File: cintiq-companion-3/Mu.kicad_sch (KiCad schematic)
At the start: 12 parts, among them J1 Conn_01x03_Pin

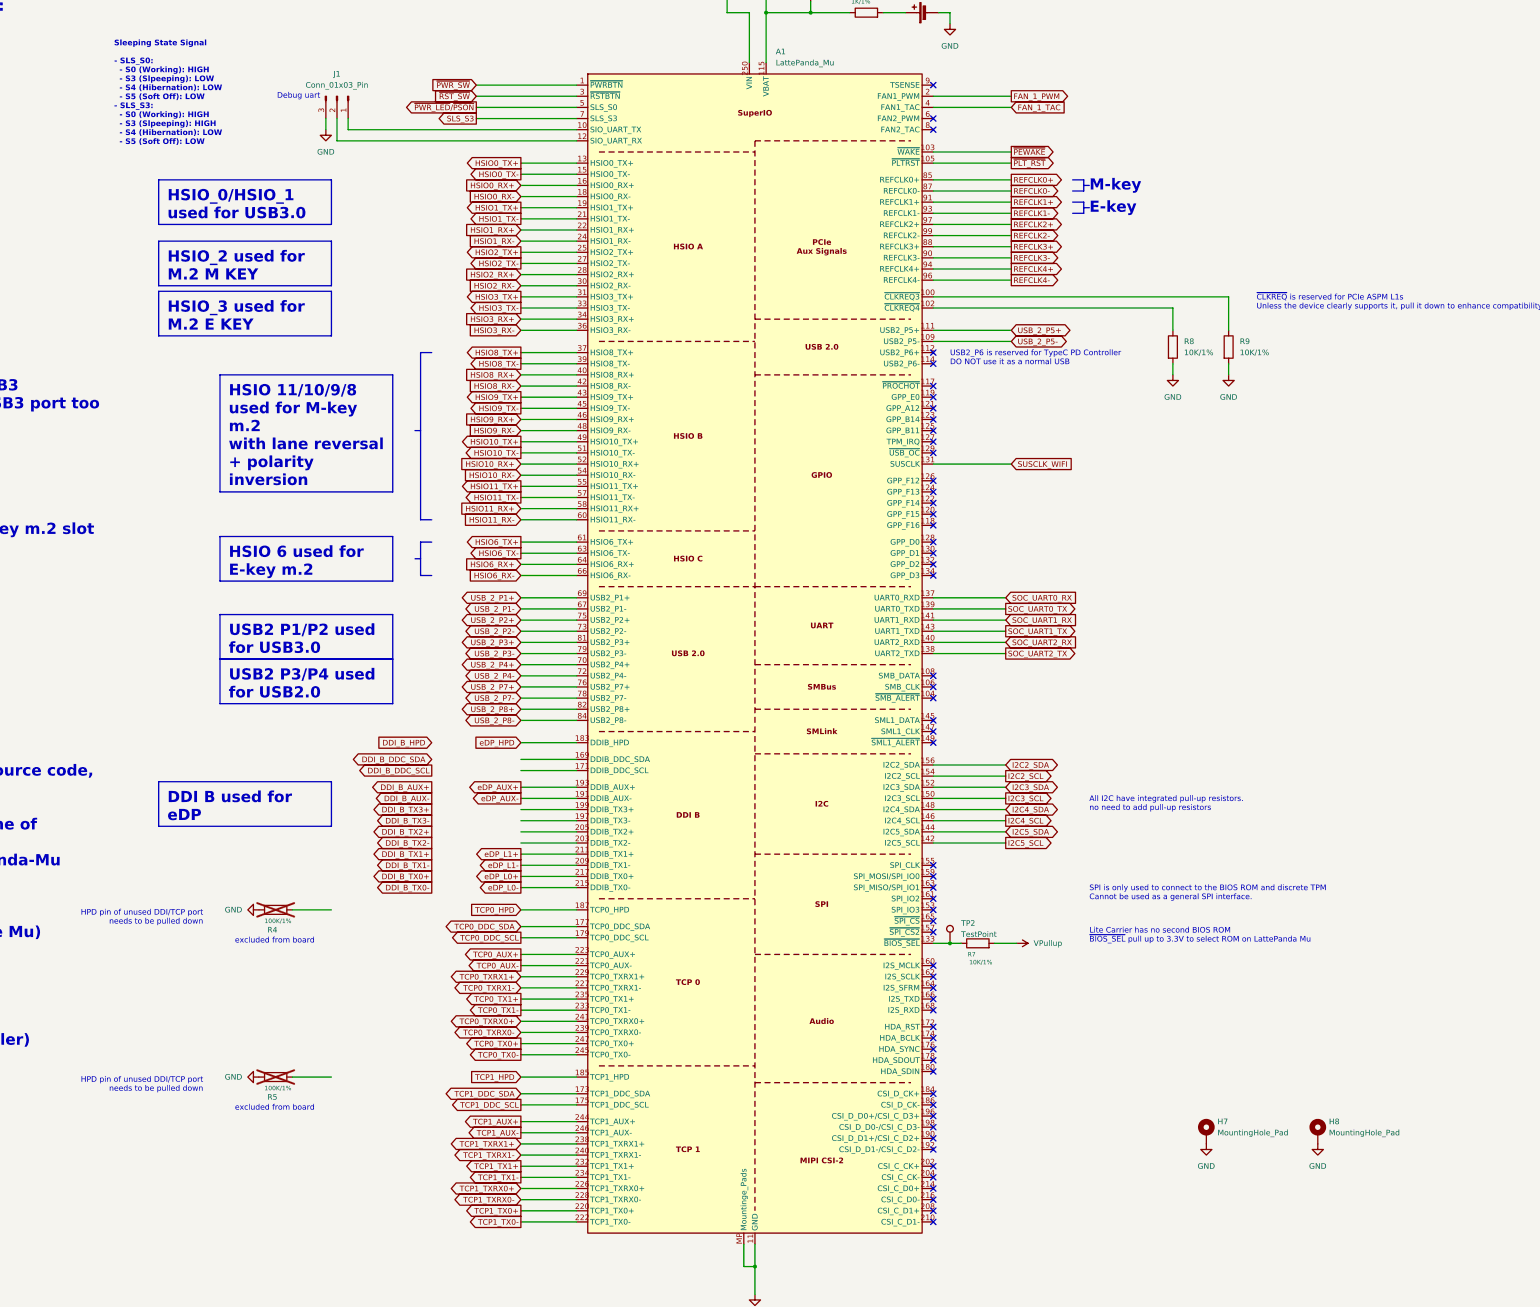
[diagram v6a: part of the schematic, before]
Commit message: Disconnected so far unused things on schematic
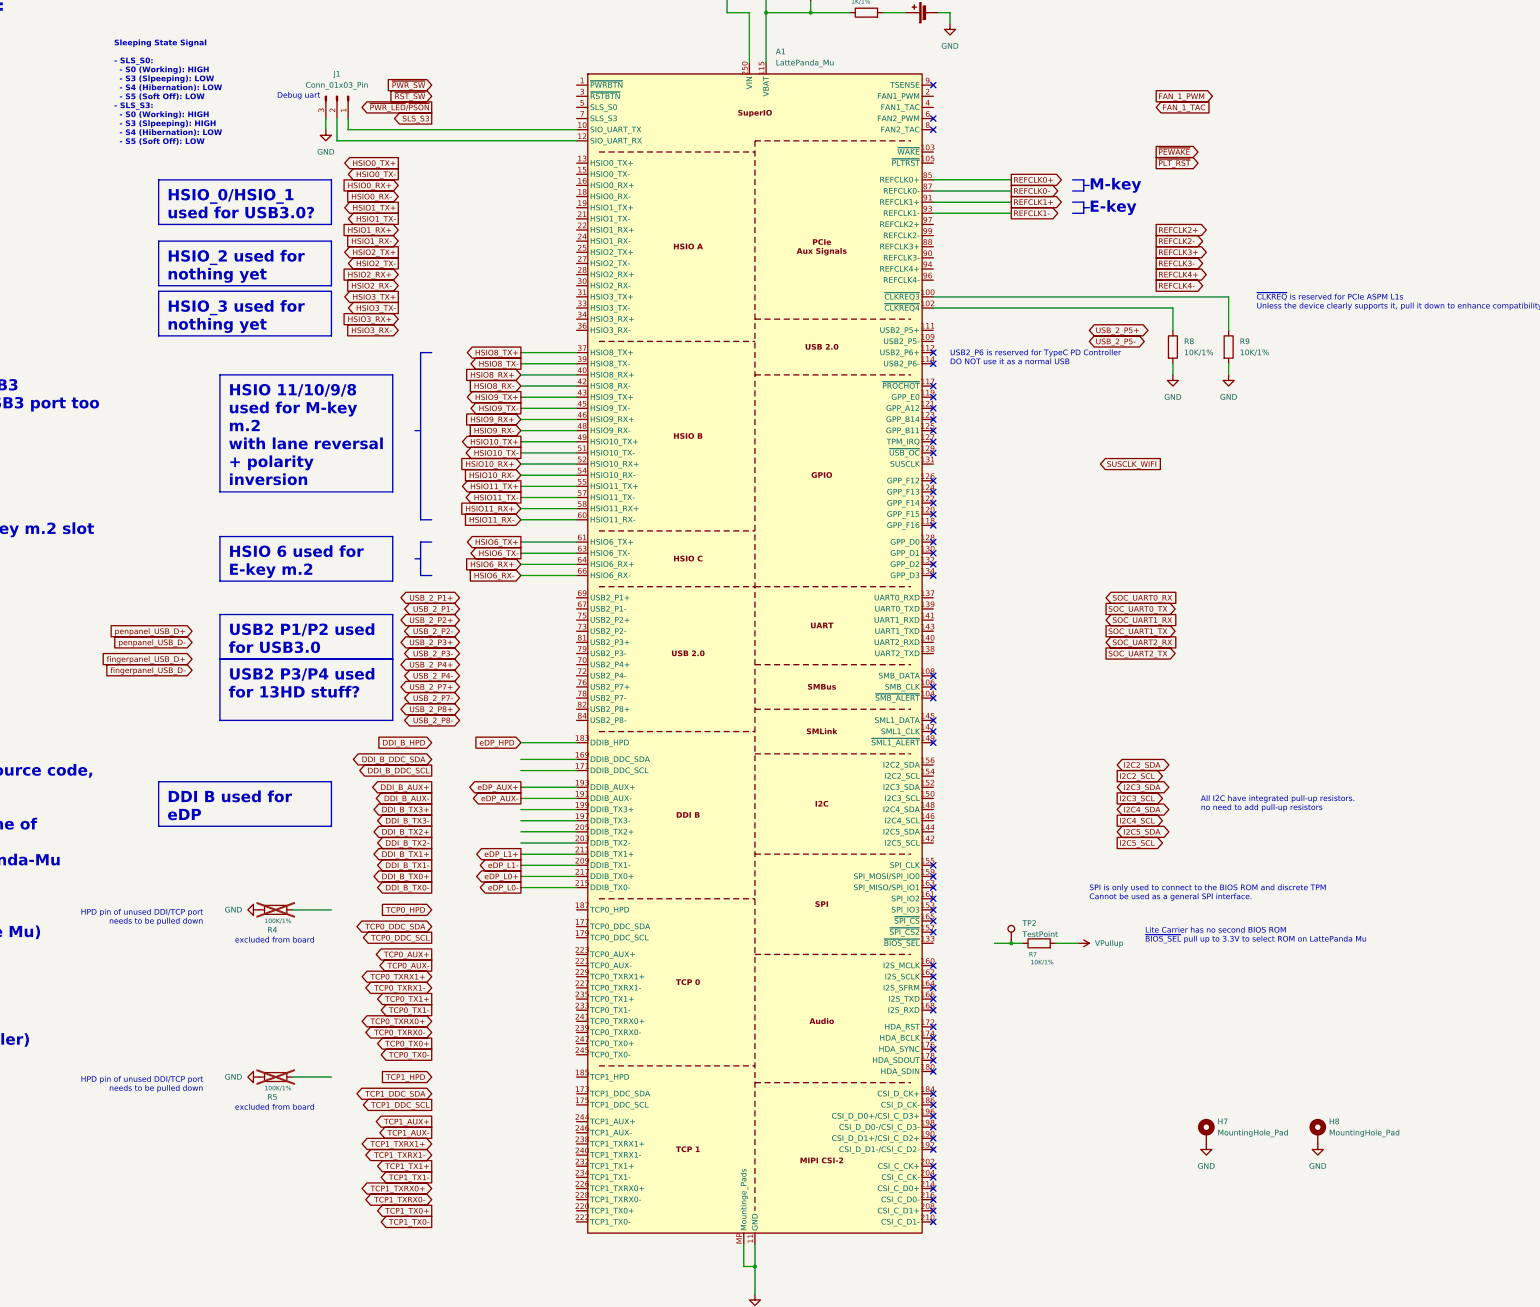
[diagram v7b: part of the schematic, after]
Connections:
- net FAN_1_PWM: no longer A1.2 (FAN1_PWM)
- net FAN_1_TAC: no longer A1.4 (FAN1_TAC)
- net HSIO0_RX+: no longer A1.16 (HSIO0_RX+)
- net HSIO0_RX-: no longer A1.18 (HSIO0_RX-)
- net HSIO0_TX+: no longer A1.13 (HSIO0_TX+)
- net HSIO0_TX-: no longer A1.15 (HSIO0_TX-)
- net HSIO1_RX+: no longer A1.22 (HSIO1_RX+)
- net HSIO1_RX-: no longer A1.24 (HSIO1_RX-)
- net HSIO1_TX+: no longer A1.19 (HSIO1_TX+)
- net HSIO1_TX-: no longer A1.21 (HSIO1_TX-)
- net HSIO2_RX+: no longer A1.28 (HSIO2_RX+)
- net HSIO2_RX-: no longer A1.30 (HSIO2_RX-)
- net HSIO2_TX+: no longer A1.25 (HSIO2_TX+)
- net HSIO2_TX-: no longer A1.27 (HSIO2_TX-)
- net HSIO3_RX+: no longer A1.34 (HSIO3_RX+)
- net HSIO3_RX-: no longer A1.36 (HSIO3_RX-)
- net HSIO3_TX+: no longer A1.31 (HSIO3_TX+)
- net HSIO3_TX-: no longer A1.33 (HSIO3_TX-)
- net I2C2_SCL: no longer A1.154 (I2C2_SCL)
- net I2C2_SDA: no longer A1.156 (I2C2_SDA)
- net I2C3_SCL: no longer A1.150 (I2C3_SCL)
- net I2C3_SDA: no longer A1.152 (I2C3_SDA)
- net I2C4_SCL: no longer A1.146 (I2C4_SCL)
- net I2C4_SDA: no longer A1.148 (I2C4_SDA)
- net I2C5_SCL: no longer A1.142 (I2C5_SCL)
- net I2C5_SDA: no longer A1.144 (I2C5_SDA)
- net REFCLK2+: no longer A1.97 (REFCLK2+)
- net REFCLK2-: no longer A1.99 (REFCLK2-)
- net REFCLK3+: no longer A1.88 (REFCLK3+)
- net REFCLK3-: no longer A1.90 (REFCLK3-)
- net REFCLK4+: no longer A1.94 (REFCLK4+)
- net REFCLK4-: no longer A1.96 (REFCLK4-)
- net SLS_S3: no longer A1.7 (SLS_S3)
- net SOC_UART0_RX: no longer A1.137 (UART0_RXD)
- net SOC_UART0_TX: no longer A1.139 (UART0_TXD)
- net SOC_UART1_RX: no longer A1.141 (UART1_RXD)
- net SOC_UART1_TX: no longer A1.143 (UART1_TXD)
- net SOC_UART2_RX: no longer A1.140 (UART2_RXD)
- net SOC_UART2_TX: no longer A1.138 (UART2_TXD)
- net SUSCLK_WIFI: no longer A1.131 (SUSCLK)
- net TCP0_AUX+: no longer A1.223 (TCP0_AUX+)
- net TCP0_AUX-: no longer A1.221 (TCP0_AUX-)
- net TCP0_DDC_SCL: no longer A1.179 (TCP0_DDC_SCL)
- net TCP0_DDC_SDA: no longer A1.177 (TCP0_DDC_SDA)
- net TCP0_HPD: no longer A1.187 (TCP0_HPD)
- net TCP0_TX0+: no longer A1.247 (TCP0_TX0+)
- net TCP0_TX0-: no longer A1.245 (TCP0_TX0-)
- net TCP0_TX1+: no longer A1.235 (TCP0_TX1+)
- net TCP0_TX1-: no longer A1.233 (TCP0_TX1-)
- net TCP0_TXRX0+: no longer A1.241 (TCP0_TXRX0+)
- net TCP0_TXRX0-: no longer A1.239 (TCP0_TXRX0-)
- net TCP0_TXRX1+: no longer A1.229 (TCP0_TXRX1+)
- net TCP0_TXRX1-: no longer A1.227 (TCP0_TXRX1-)
- net TCP1_AUX+: no longer A1.244 (TCP1_AUX+)
- net TCP1_AUX-: no longer A1.246 (TCP1_AUX-)
- net TCP1_DDC_SCL: no longer A1.175 (TCP1_DDC_SCL)
- net TCP1_DDC_SDA: no longer A1.173 (TCP1_DDC_SDA)
- net TCP1_HPD: no longer A1.185 (TCP1_HPD)
- net TCP1_TX0+: no longer A1.220 (TCP1_TX0+)
- net TCP1_TX0-: no longer A1.222 (TCP1_TX0-)
- net TCP1_TX1+: no longer A1.232 (TCP1_TX1+)
- net TCP1_TX1-: no longer A1.234 (TCP1_TX1-)
- net TCP1_TXRX0+: no longer A1.226 (TCP1_TXRX0+)
- net TCP1_TXRX0-: no longer A1.228 (TCP1_TXRX0-)
- net TCP1_TXRX1+: no longer A1.238 (TCP1_TXRX1+)
- net TCP1_TXRX1-: no longer A1.240 (TCP1_TXRX1-)
- net USB_2_P1+: no longer A1.69 (USB2_P1+)
- net USB_2_P1-: no longer A1.67 (USB2_P1-)
- net USB_2_P2+: no longer A1.75 (USB2_P2+)
- net USB_2_P2-: no longer A1.73 (USB2_P2-)
- net USB_2_P3+: no longer A1.81 (USB2_P3+)
- net USB_2_P3-: no longer A1.79 (USB2_P3-)
- net USB_2_P4+: no longer A1.70 (USB2_P4+)
- net USB_2_P4-: no longer A1.72 (USB2_P4-)
- net USB_2_P5+: no longer A1.111 (USB2_P5+)
- net USB_2_P5-: no longer A1.109 (USB2_P5-)
- net USB_2_P7+: no longer A1.76 (USB2_P7+)
- net USB_2_P7-: no longer A1.78 (USB2_P7-)
- net USB_2_P8+: no longer A1.82 (USB2_P8+)
- net USB_2_P8-: no longer A1.84 (USB2_P8-)
- net ~{PEWAKE}: no longer A1.103 (~{WAKE})
- net ~{PLT_RST}: no longer A1.105 (~{PLTRST})
- net ~{PWR_LED}/~{PSON}: no longer A1.5 (SLS_S0)
- net ~{PWR_SW}: no longer A1.1 (~{PWRBTN})
- net ~{RST_SW}: no longer A1.3 (~{RSTBTN})
- net at R7.1, TP2.1: no longer A1.133 (~{BIOS_SEL})
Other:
- moved on the sheet: R7, TP2
